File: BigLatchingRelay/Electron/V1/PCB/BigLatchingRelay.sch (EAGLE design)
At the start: 11 parts, among them IC2 BD6211F

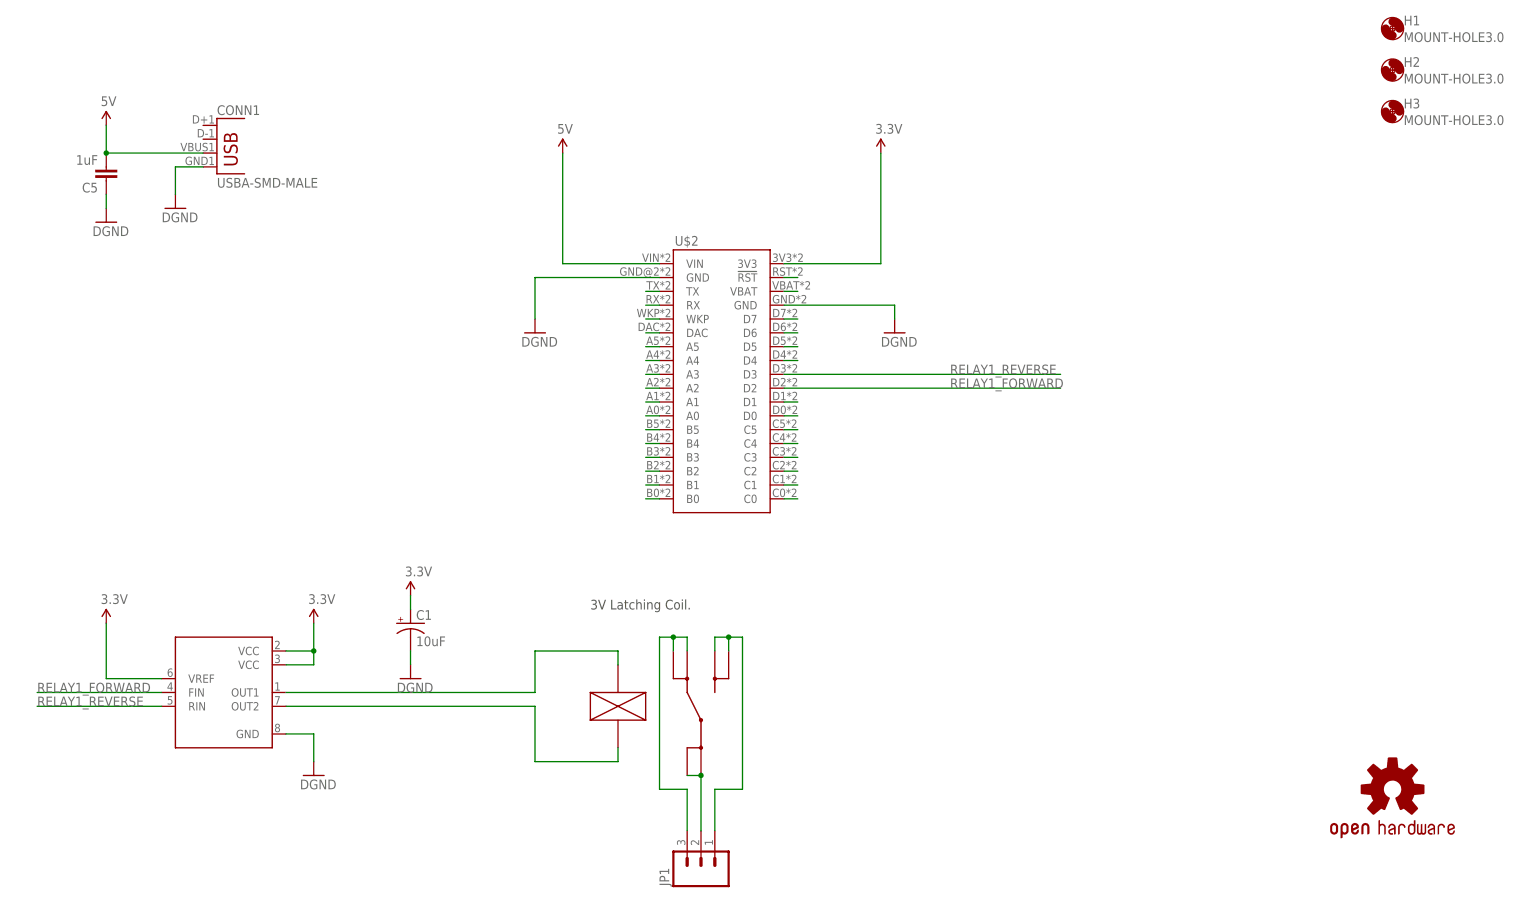
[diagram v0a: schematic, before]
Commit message: Renamed BigLatchingRelay. Updated to V2.1: Moved connector to end rather than side to reduce strain on one side when USB A connector used. Added OSH Logo LED (and bigger OSH Logo). Added high volage warning text to board top and bottom. Added PDFs of board and schematic.
Added DirtyPcb images.
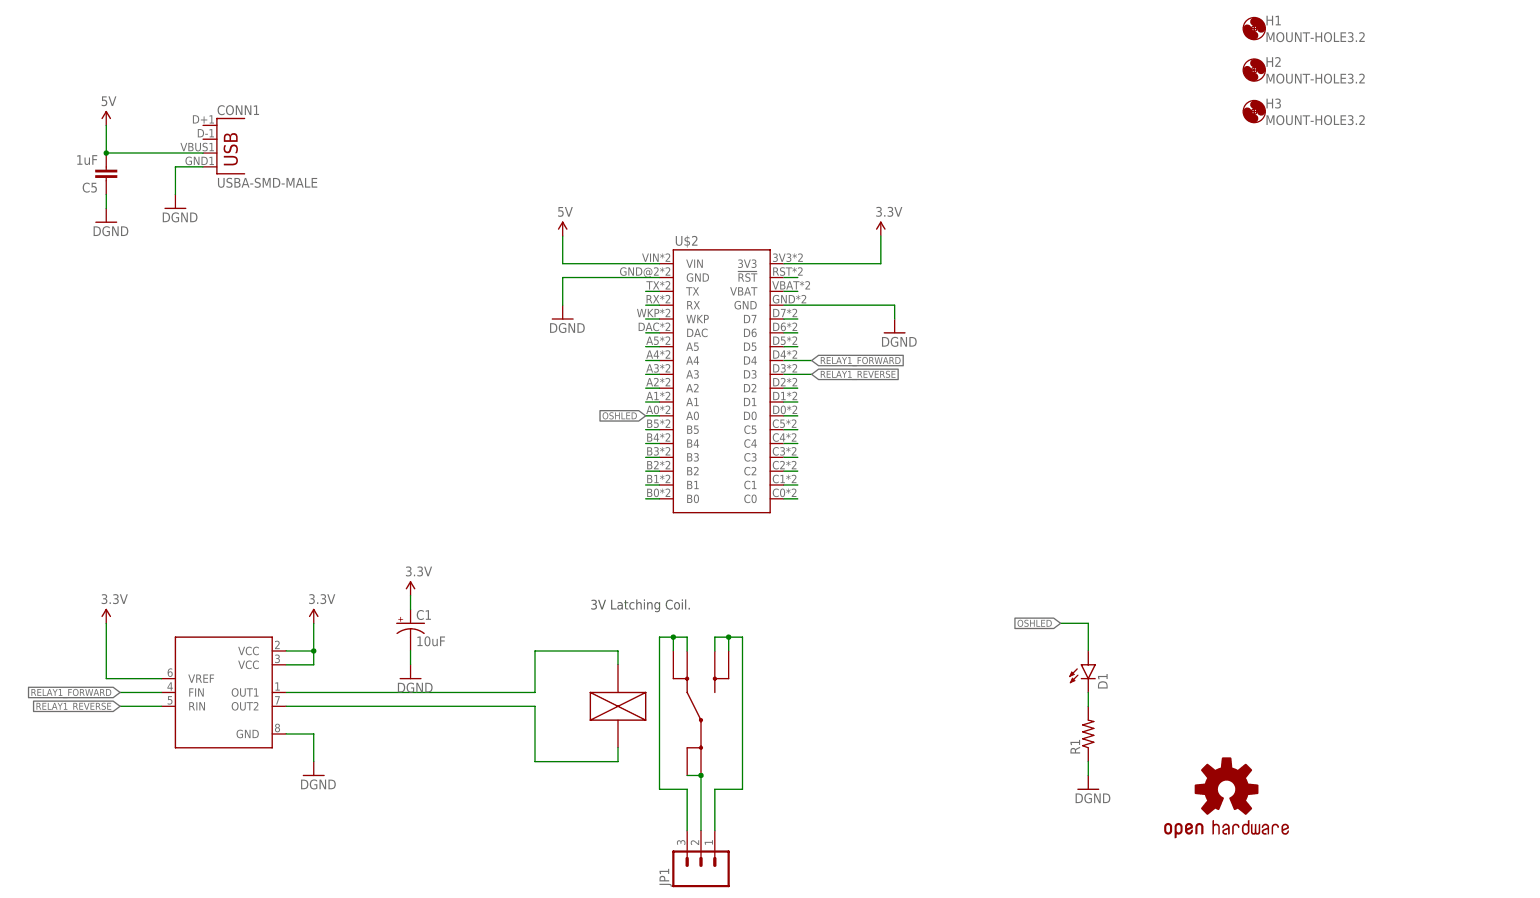
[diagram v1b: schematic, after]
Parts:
- removed LOGO2: OSHW-LOGOS, SparkFun-Aesthetics:OSHW-LOGOS
- added D1: (no value), SparkFun-LED:LED1206-BOTTOM
- added LOGO1: OSHW-LOGOM, SparkFun-Aesthetics:OSHW-LOGOM
- added R1: (no value), SparkFun-Resistors:RESISTOR1206
- H1, H2, H3: value MOUNT-HOLE3.0 -> MOUNT-HOLE3.2; device holes:MOUNT-HOLE3.0 -> holes:MOUNT-HOLE3.2
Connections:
- removed net N$39 (its old number): U$2.A0
- new net N$11: D1.C, R1.2
- new net OSHLED: D1.A, U$2.A0
- net GND: now also R1.1
- net N$20: now also U$2.D2; no longer U$2.D4
- net RELAY1_FORWARD: now also U$2.D4; no longer U$2.D2
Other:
- moved on the sheet: H1, H2, H3

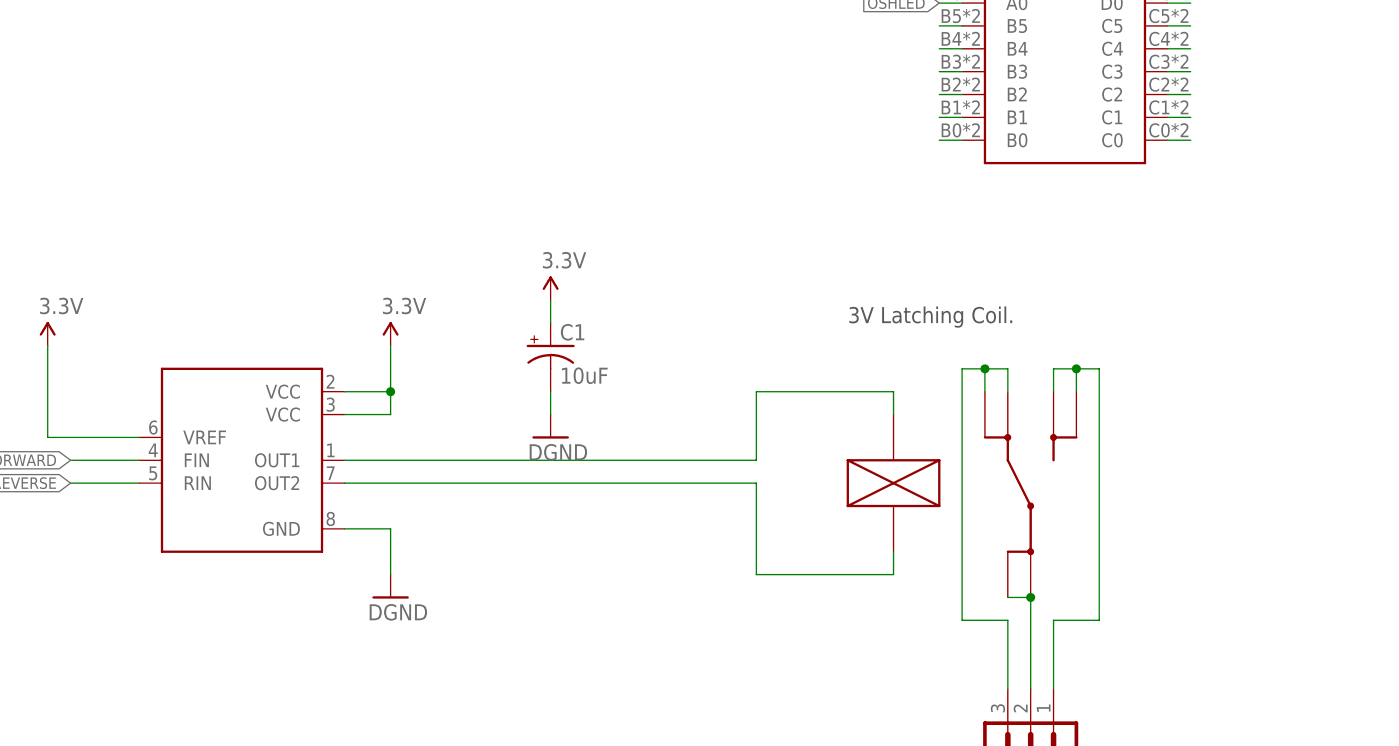
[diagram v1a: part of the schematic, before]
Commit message: Added datasheets for relay and relay driver.
Improved text on schematic.
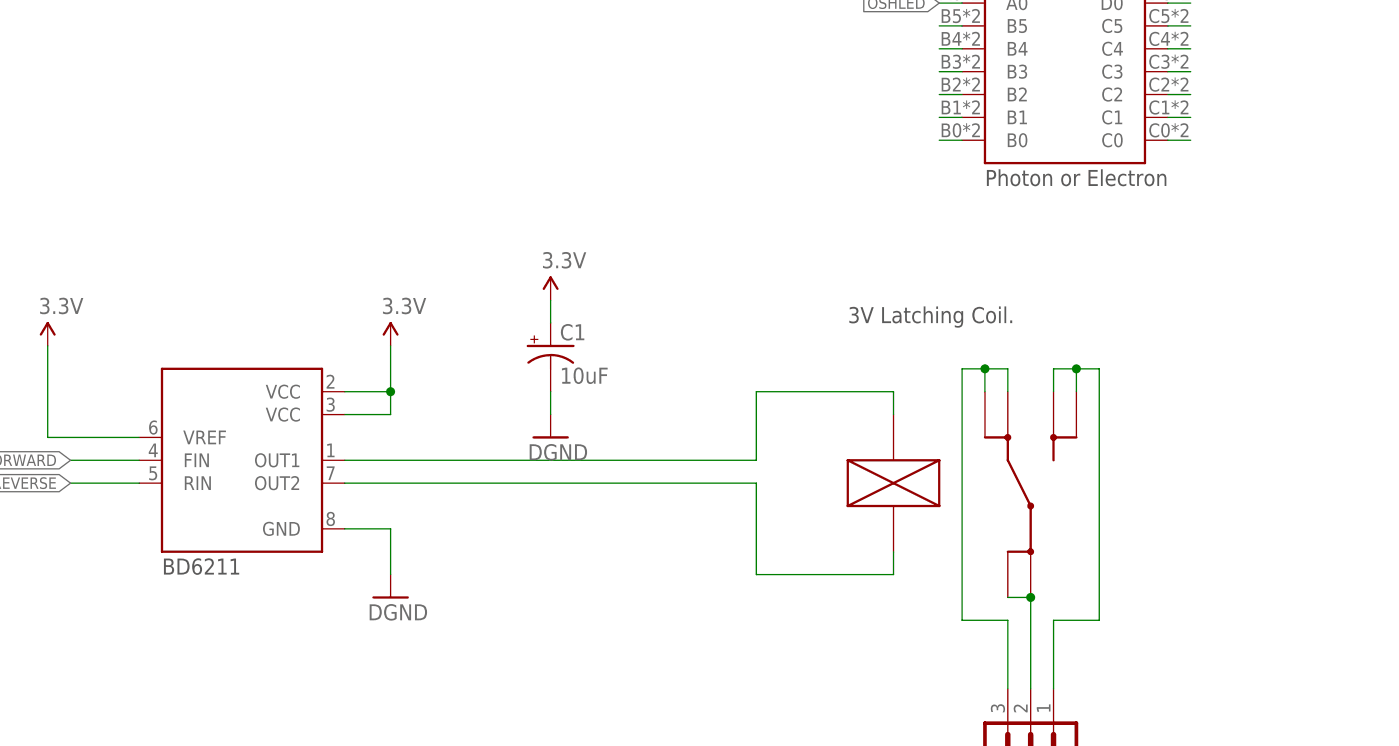
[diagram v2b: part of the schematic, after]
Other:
- note added: "BD6211"
- note added: "Photon or Electron"
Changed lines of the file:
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@@
 <plain>
 <text x="111.76" y="73.66" size="1.778" layer="97">3V Latching Coil.</text>
+<text x="35.56" y="45.72" size="1.778" layer="97">BD6211</text>
+<text x="127" y="88.9" size="1.778" layer="97">Photon or Electron</text>
 </plain>
 <instances>

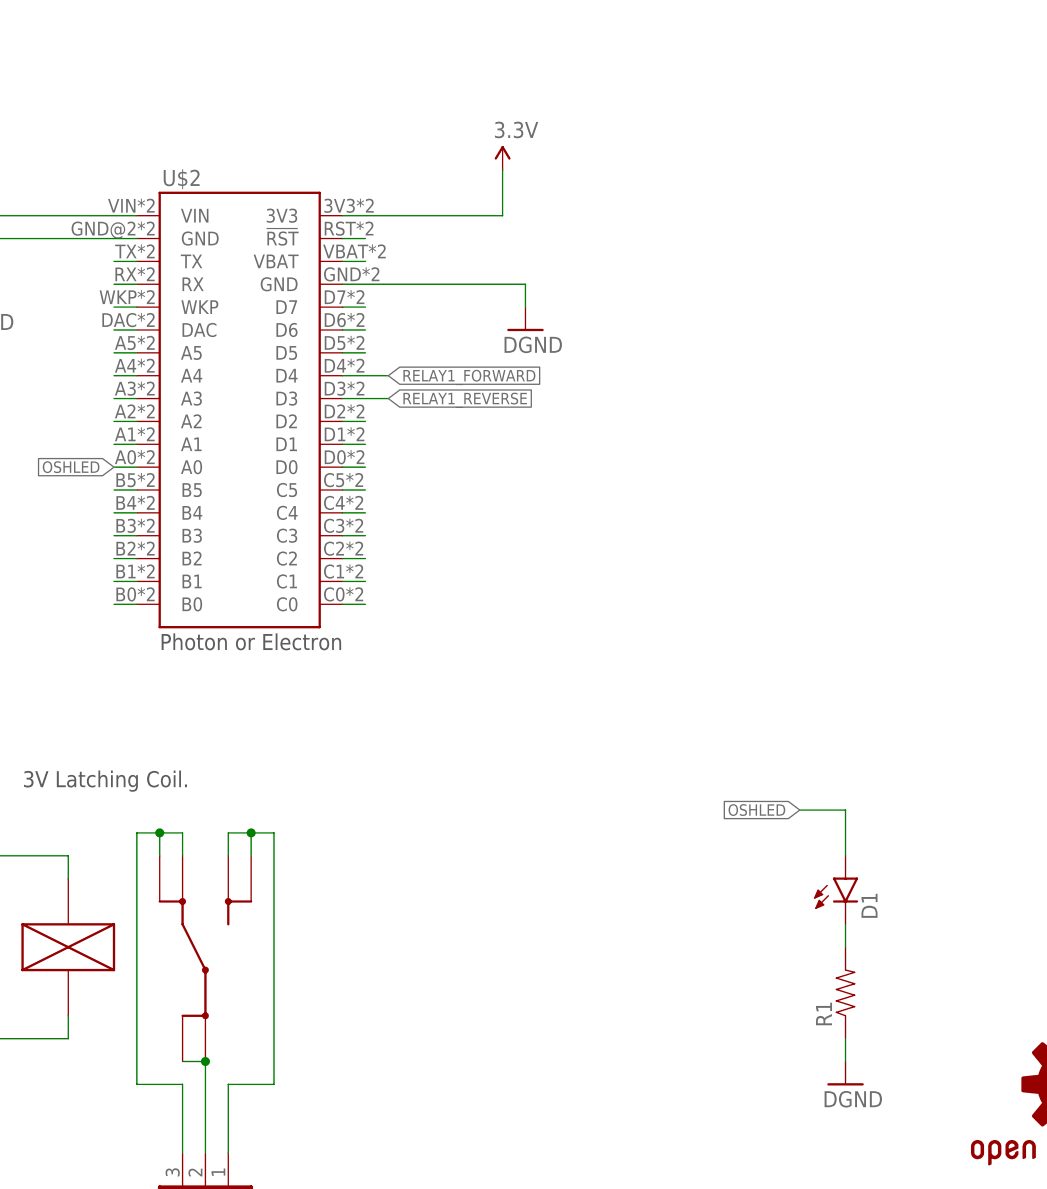
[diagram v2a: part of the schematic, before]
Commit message: Updated part identifiers and added BOMs
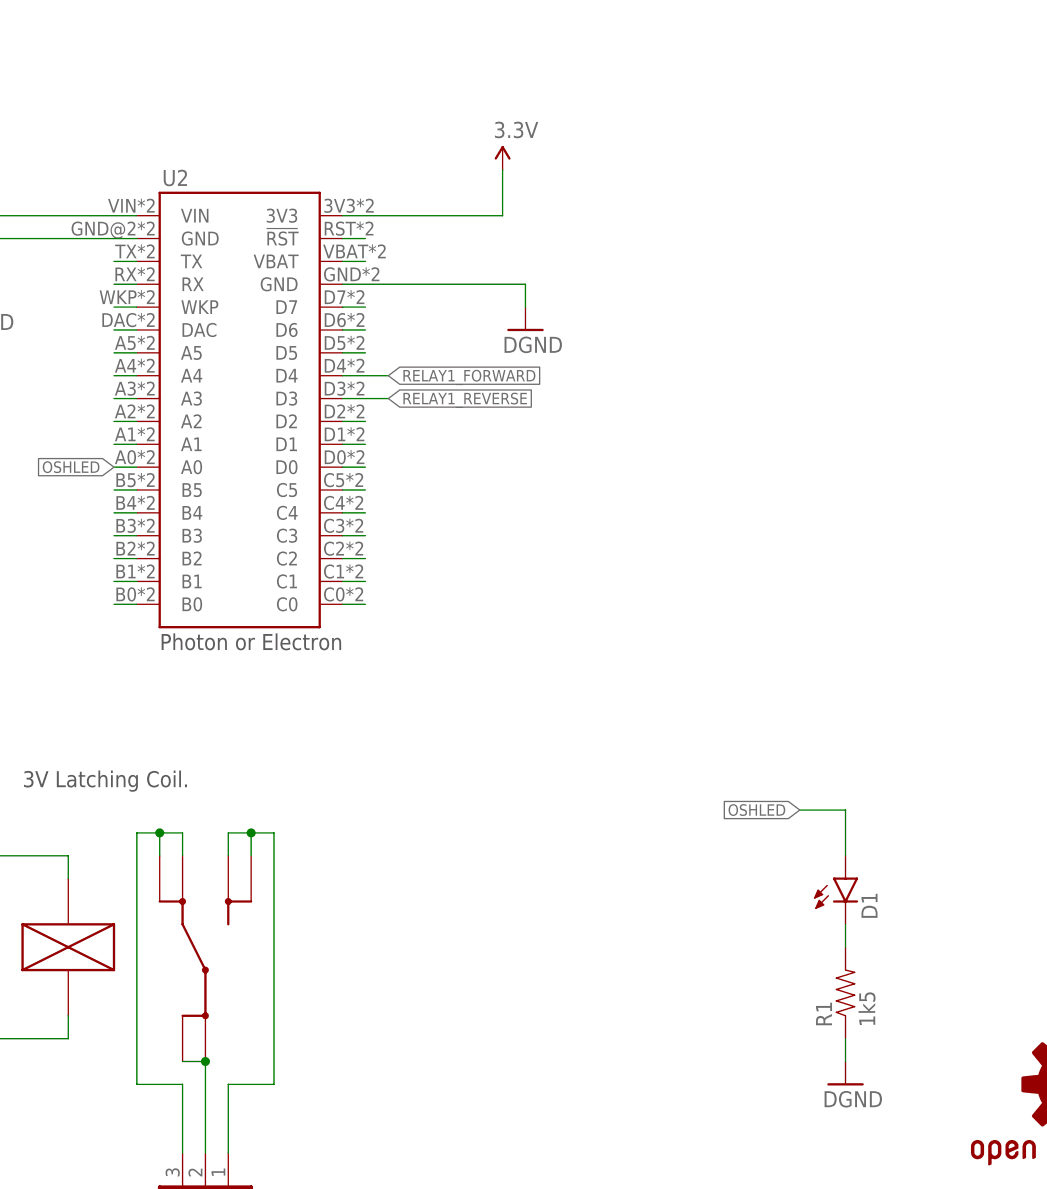
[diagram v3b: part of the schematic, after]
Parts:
- R1: value (none) -> 1k5
- renumbered IC2 to U3, U$2 to U2
